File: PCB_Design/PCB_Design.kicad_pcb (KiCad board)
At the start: 2 copper layers, 97.6 x 69.4 mm, 58 parts, among them IC1 MIC37303YME, J1 TP4056, J2 632723300011, SW1 SW_Push, SW2 SW_Push, U1 ESP32-WROOM-32

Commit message: PCB diseño fianl retocado + lista componentes
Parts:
- added C_bypass1: 100pF, Capacitor_SMD:C_0805_2012Metric_Pad1.18x1.45mm_HandSolder, F.Cu at (149.6, 127.1)
- Conn_I2C1: value Conn_01x03_Female -> Conn_01x04_Female; footprint Connector_PinSocket_2.54mm:PinSocket_1x03_P2.54mm_Vertical_SMD_Pin1Left -> Connector_PinSocket_2.54mm:PinSocket_1x04_P2.54mm_Vertical_SMD_Pin1Left
- moved Conn_I2C1 1.34 mm to (67.1, 120.5), turned to 180 degrees
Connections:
- Conn_I2C1 pad 1: GND -> Net-(Conn_I2C1-Pad1)
- Conn_I2C1 pad 3: Net-(Conn_I2C1-Pad3) -> GND
- Conn_OLED1 pad 4: Net-(Conn_I2C1-Pad3) -> Net-(Conn_I2C1-Pad1)
- U1 pad 33: Net-(Conn_I2C1-Pad3) -> Net-(Conn_I2C1-Pad1)
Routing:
- net Net-(Conn_I2C1-Pad3): track 149.5 -> 0.00 mm
- net Net-(Conn_I2C1-Pad1): track 0.00 -> 149.5 mm
- net /3.3v: track 203.6 -> 229.8 mm
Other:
- board text added: "3V3"
- board text added: "DAT"
- board text added: "GND"
- board text added: "NC"
- board text added: "RX"
- board text added: "SCL"
- board text added: "SDA"
- board text added: "TX"

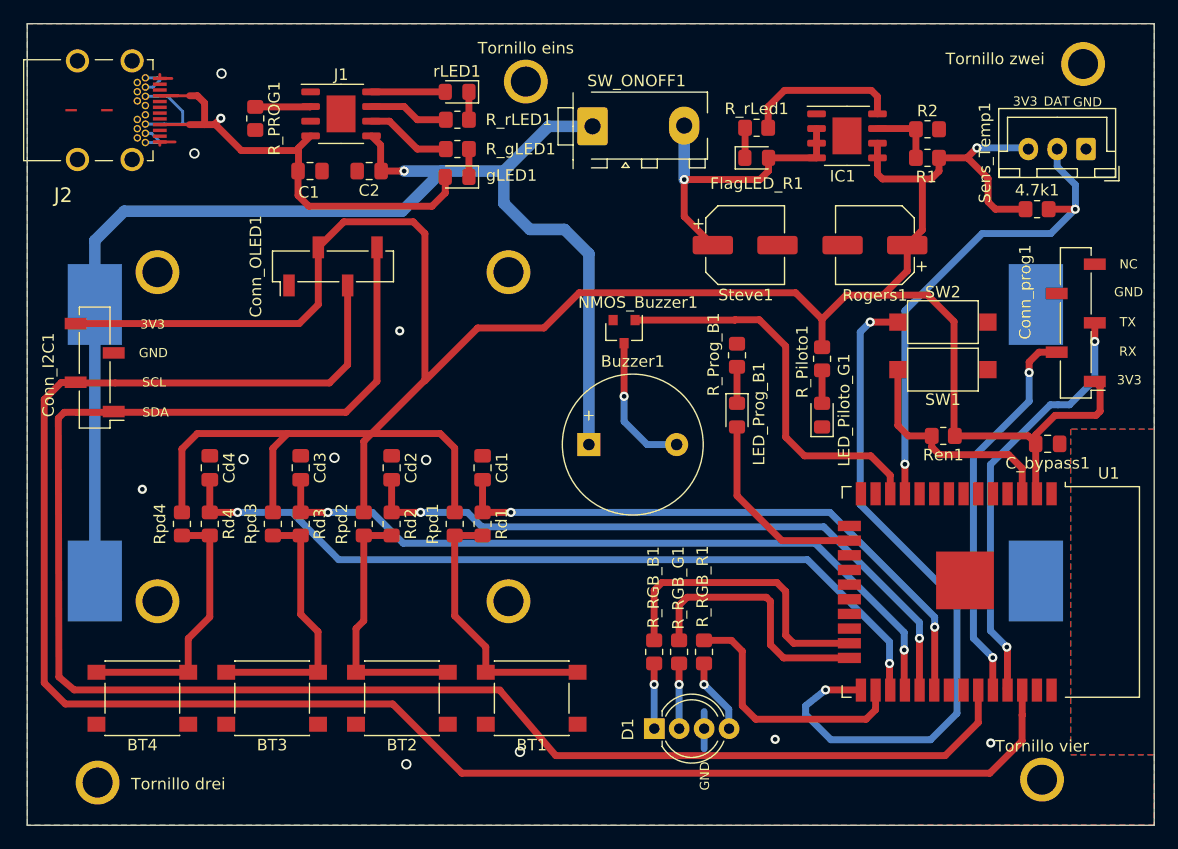
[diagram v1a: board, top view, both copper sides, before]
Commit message: PCB final con usb B micro, y modelo 3D de la placa
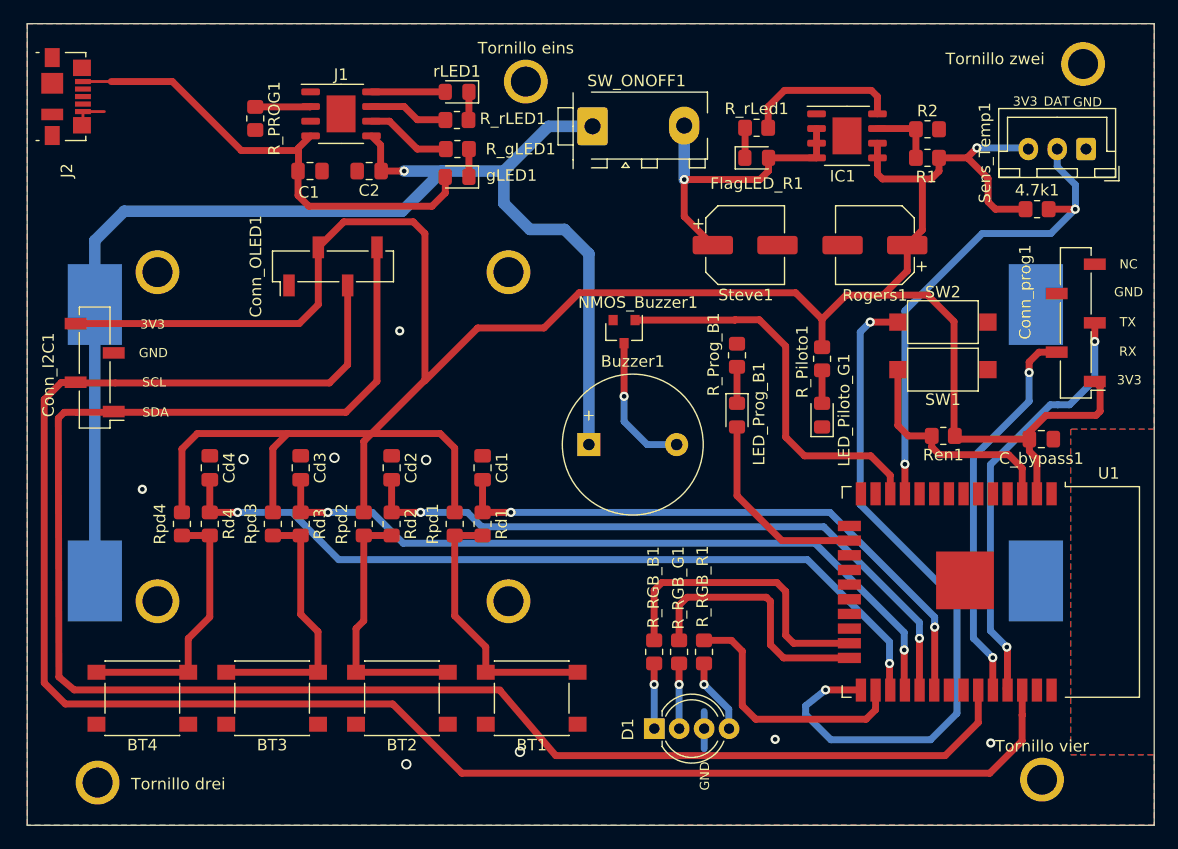
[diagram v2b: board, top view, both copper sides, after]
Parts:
- J2: value 632723300011 -> USB_B_Micro; footprint Connector_USB:632723300011 -> Connector_USB:USB_Micro-B_Molex_47346-0001
- moved J2 2.52 mm to (64.6, 97.1)
- moved C_bypass1 0.68 mm to (149.0, 126.7)
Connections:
- J2 pad 1: GND -> Net-(C1-Pad1)
- J2 pad 2: GND -> Net-(J2-Pad2)
- J2 pad 5: Net-(J2-Pad5) -> GND
- J2 pad 6: Net-(J2-Pad6) -> GND
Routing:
- net Net-(C1-Pad1): track 53.5 -> 41.8 mm, vias 1 -> 0
- net GND: track 11.9 -> 6.30 mm, vias 11 -> 9

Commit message: PCB terminada
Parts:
- Cd1, Cd2, Cd3, Cd4: value 1u -> 0.1u
- R1: value 1M -> 6.98k; footprint Resistor_SMD:R_0805_2012Metric_Pad1.20x1.40mm_HandSolder -> Resistor_SMD:R_1206_3216Metric_Pad1.30x1.75mm_HandSolder
- R2: value 590k -> 4.02k; footprint Resistor_SMD:R_0805_2012Metric_Pad1.20x1.40mm_HandSolder -> Resistor_SMD:R_1206_3216Metric_Pad1.30x1.75mm_HandSolder
- R_PROG1: value R -> 4.7k
- moved R2 0.56 mm to (139.4, 99.4)
- moved R1 0.26 mm to (139.4, 102.3)
